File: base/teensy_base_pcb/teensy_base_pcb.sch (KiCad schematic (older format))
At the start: 24 parts, among them U1 LM7805CT, U2 LD1117V33, U3 Teensy_3.2, U4 nRF24L01+, U5 TA8428K

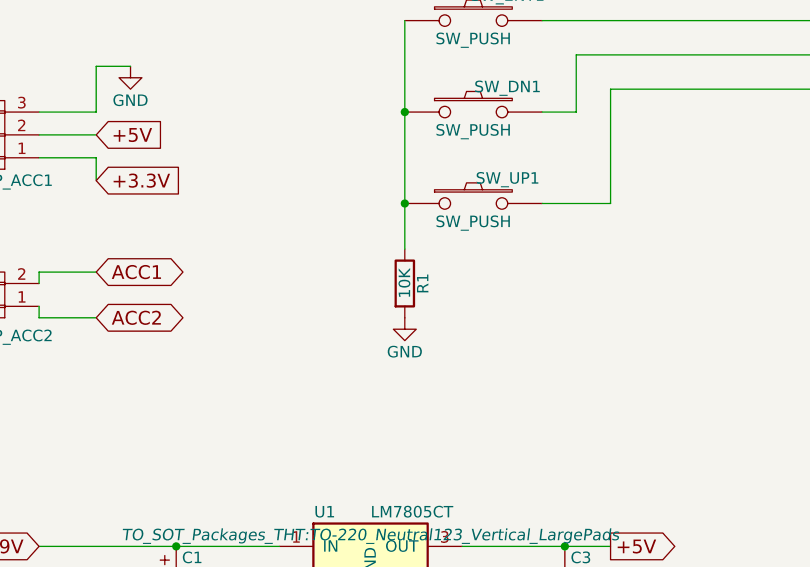
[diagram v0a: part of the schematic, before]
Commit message: Add document title / rev and set button R value.
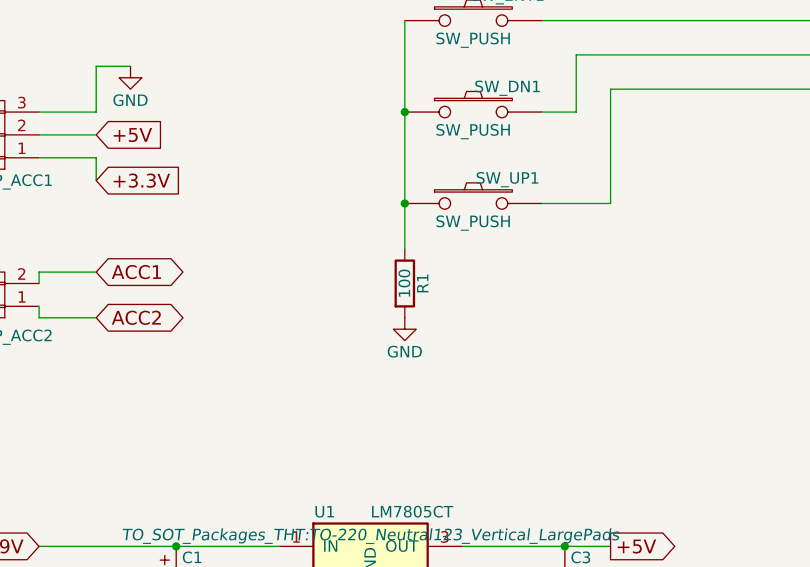
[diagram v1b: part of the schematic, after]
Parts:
- R1: value 10K -> 100
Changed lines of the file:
@@
 encoding utf-8
 Sheet 1 1
-Title ""
+Title "Teensy Base PCB"
 Date ""
-Rev ""
+Rev "1a"
 Comp ""
 Comment1 ""
@@
 P 2650 3900
 F 0 "R1" V 2730 3900 50  0000 C CNN
-F 1 "10K" V 2650 3900 50  0000 C CNN
+F 1 "100" V 2650 3900 50  0000 C CNN
 F 2 "Resistors_ThroughHole:Resistor_Horizontal_RM10mm" V 2580 3900 50  0001 C CNN
 F 3 "" H 2650 3900 50  0000 C CNN
